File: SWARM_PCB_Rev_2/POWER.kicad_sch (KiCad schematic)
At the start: 54 parts

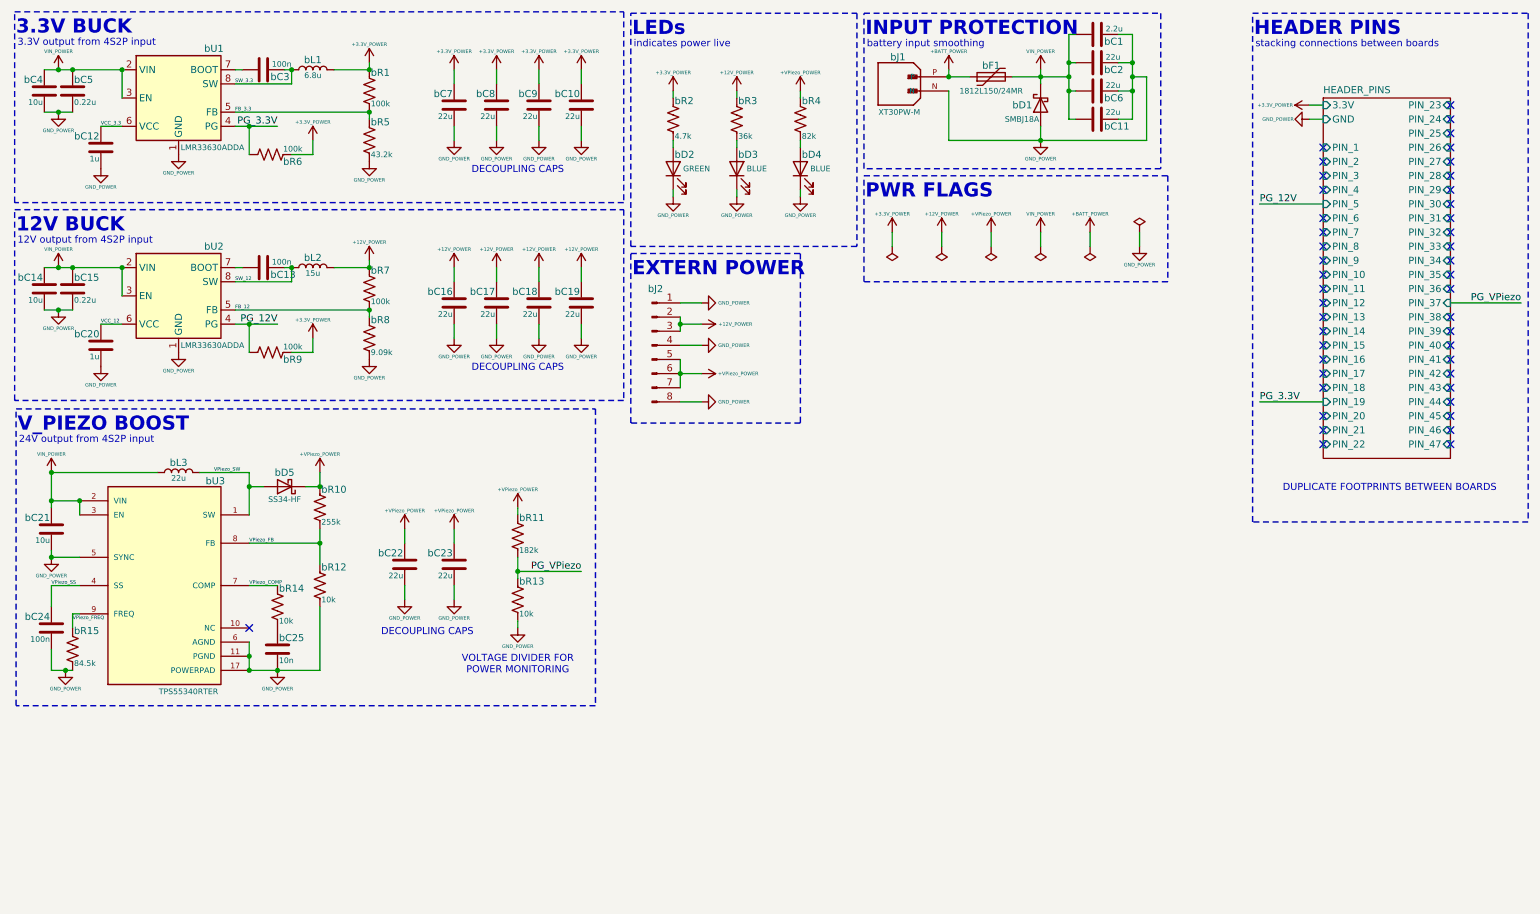
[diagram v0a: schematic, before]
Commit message: Fixed some small errors and added the Output board
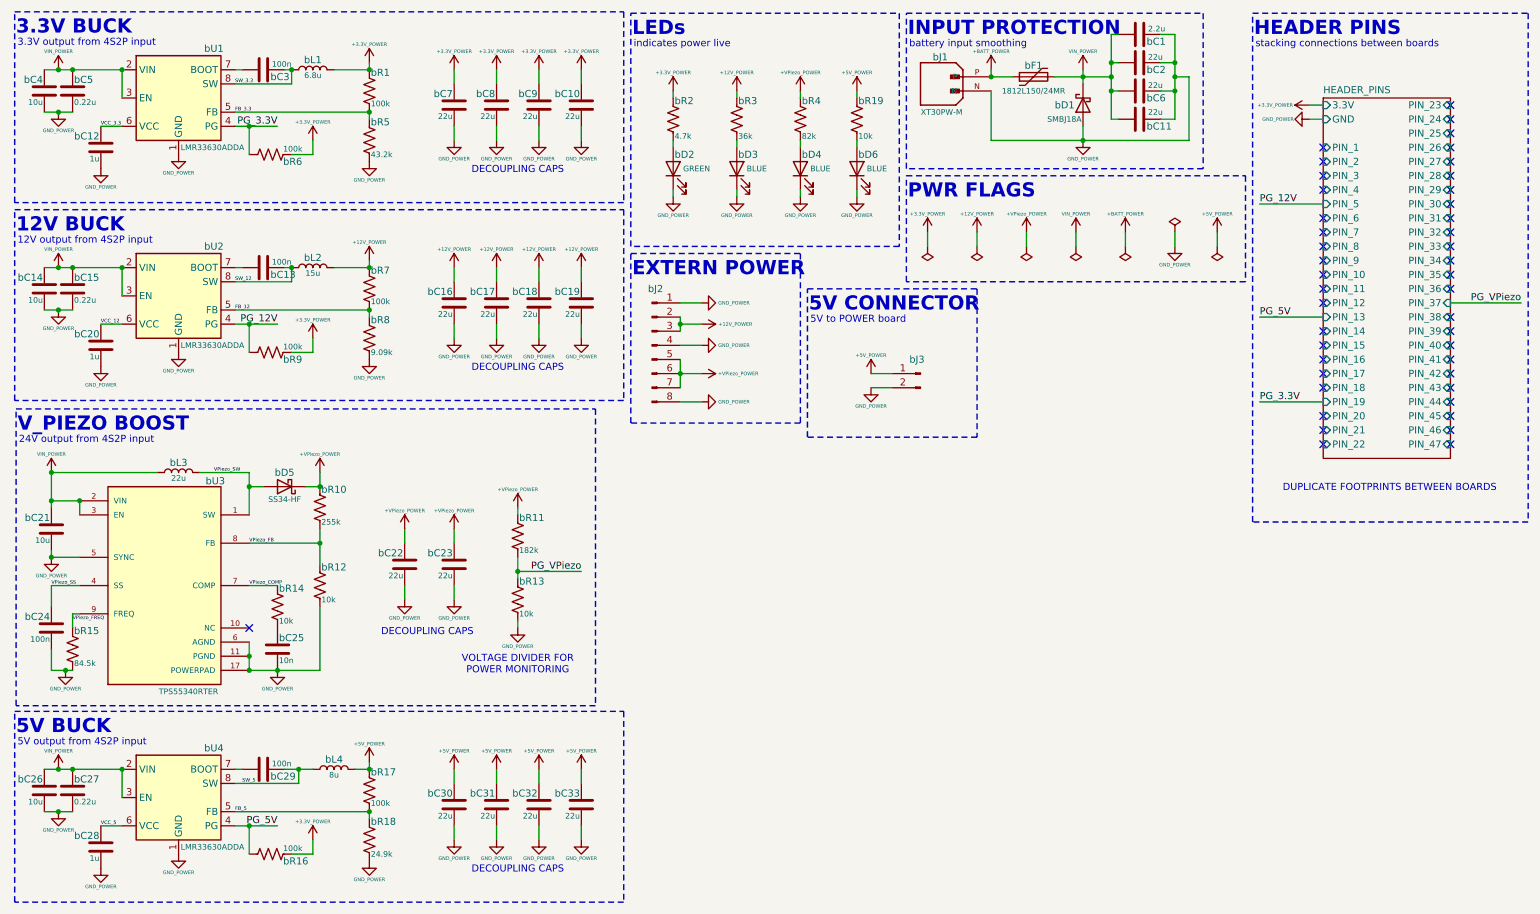
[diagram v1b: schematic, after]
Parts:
- added bC26: 10u, Capacitor_SMD:C_0805_2012Metric, symbol Device:C
- added bC27: 0.22u, Capacitor_SMD:C_0603_1608Metric, symbol Device:C
- added bC28: 1u, Capacitor_SMD:C_0603_1608Metric, symbol Device:C
- added bC29: 100n, Capacitor_SMD:C_0603_1608Metric, symbol Device:C
- added bC30, bC31, bC32, bC33: 22u, Capacitor_SMD:C_0805_2012Metric, symbol Device:C
- added bD6: BLUE, SWARM_LIBRARY:LED_JE2835_CRW, symbol Device:LED
- added bJ3: Conn_01x02_Pin, Connector_JST:JST_PH_B2B-PH-SM4-TB_1x02-1MP_P2.00mm_Vertical, symbol Connector:Conn_01x02_Pin
- added bL4: 8u, Inductor_SMD:L_Wuerth_MAPI-5030, symbol Device:L
- added bR16, bR17: 100k, Resistor_SMD:R_0603_1608Metric, symbol Device:R_US
- added bR18: 24.9k, Resistor_SMD:R_0603_1608Metric, symbol Device:R_US
- added bR19: 10k, Resistor_SMD:R_0603_1608Metric, symbol Device:R_US
- added bU4: LMR33630ADDA, Package_SO:Texas_HSOP-8-1EP_3.9x4.9mm_P1.27mm_ThermalVias, symbol Regulator_Switching:LMR33630ADDA
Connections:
- net +3.3V_POWER: now also bR16.1
- net GND_POWER: now also bC26.1, bC27.1, bC28.1, bC30.1, bC31.1, bC32.1, bC33.1, bD6.1 (K), bJ3.2 (Pin_2), bR18.1, bU4.1 (GND), bU4.9 (GND)
- net VIN_POWER: now also bC26.2, bC27.2, bU4.2 (VIN), bU4.3 (EN)
- new net: bC29.1, bU4.7 (BOOT)
- new net: bD6.2 (A), bR19.1
- new net +5V_POWER: bC30.2, bC31.2, bC32.2, bC33.2, bJ3.1 (Pin_1), bL4.2, bR17.2, bR19.2
- new net FB_5: bR17.1, bR18.2, bU4.5 (FB)
- new net PG_5V: bR16.2, bU4.4 (PG)
- new net SW_5: bC29.2, bL4.1, bU4.8 (SW)
- new net VCC_5: bC28.2, bU4.6 (VCC)
- no-connect marks 45 -> 44
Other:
- note added: "5V BUCK"
- note added: "5V CONNECTOR"
- note added: "5V output from 4S2P input"
- note added: "5V to POWER board"
- moved on the sheet: bC1, bC11, bC2, bC6, bD1, bF1, bJ1
